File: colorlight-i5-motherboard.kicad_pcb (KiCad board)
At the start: 4 copper layers, 96.5 x 96.5 mm, 76 parts, among them J1 USB C, J10 GPIO, J11 GPIO, J12 ADC_IN, J2 USB B, J3 RJ45_RB1-125B8G1A, J4 RJ45_RB1-125B8G1A, J5 Digital Video, J6 VGA, J7 GPIO, J8 Composite, J9 GPIO, U1 Colorlight i5 v7.0, U2 CH340C, U3 XC6206P332MR, U4 PI5A3157CEX, U5 AD9744, U6 GS8052-SR, U7 XC6206P332MR

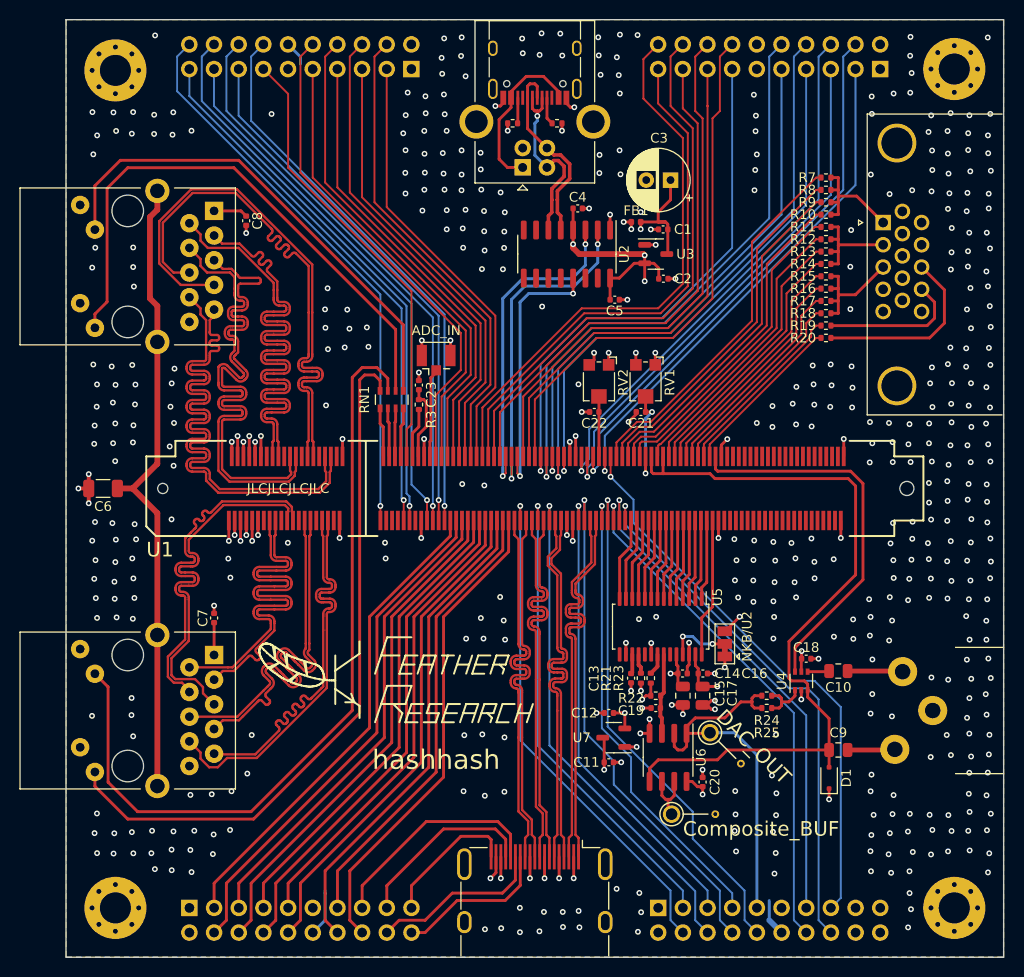
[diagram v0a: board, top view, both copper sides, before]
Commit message: Improve Ethernet skew matching
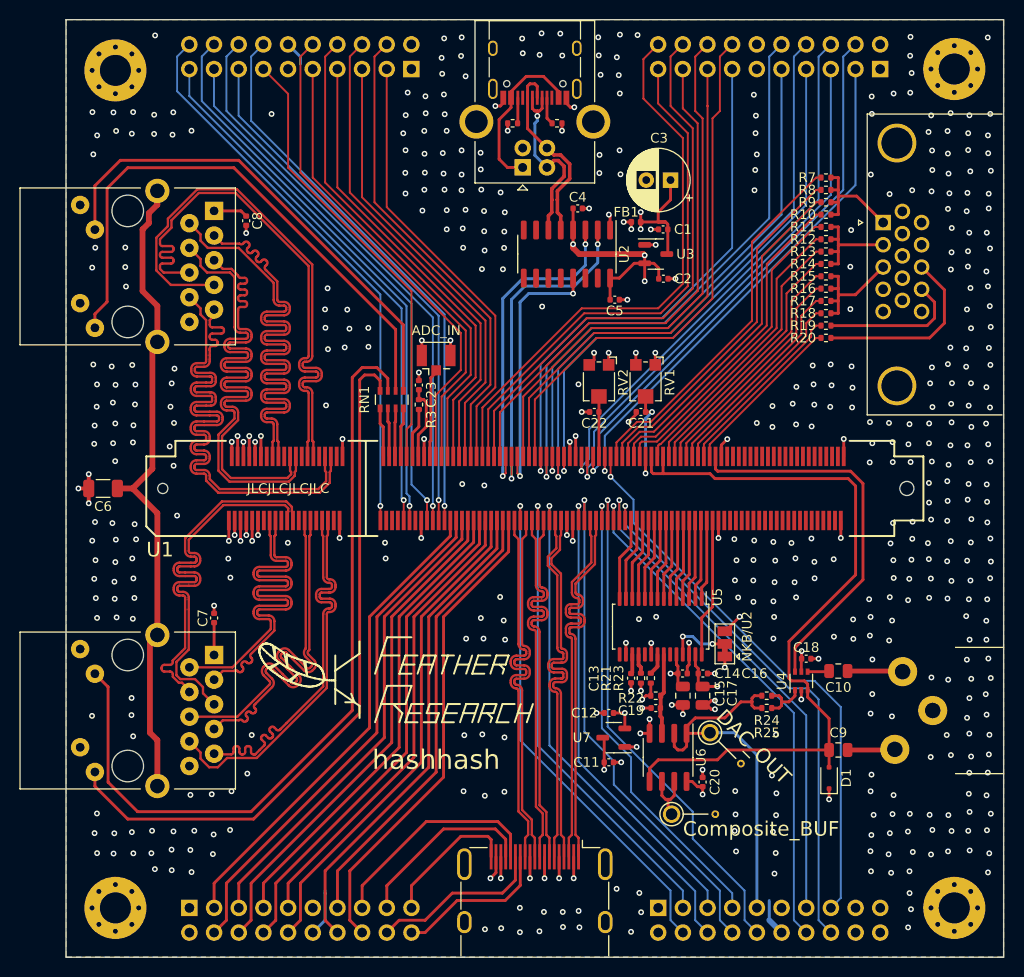
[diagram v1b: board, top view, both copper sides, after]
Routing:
- net GND: track 115.7 -> 113.8 mm
- net /Analog Video/DAC_OUT: track 39.7 -> 38.9 mm
- net Net-(U6B--): track 6.44 -> 5.67 mm
- net +5V: track 29.0 -> 29.6 mm
- net +3V3A: track 33.0 -> 32.3 mm
- net +3V3D: track 55.8 -> 55.1 mm
- net Earth: track 65.6 -> 66.1 mm
